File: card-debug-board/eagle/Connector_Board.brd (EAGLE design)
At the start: 62 x 34 mm, 39 parts, among them J1 ORESAT-DEBUG-CONNECTOR-CARD, J3 USB_A_SMT_FEMALE, Q1 MOSFET-PCH-SOT23-6, SW1 B3F-1000, U1 FT230XS-R

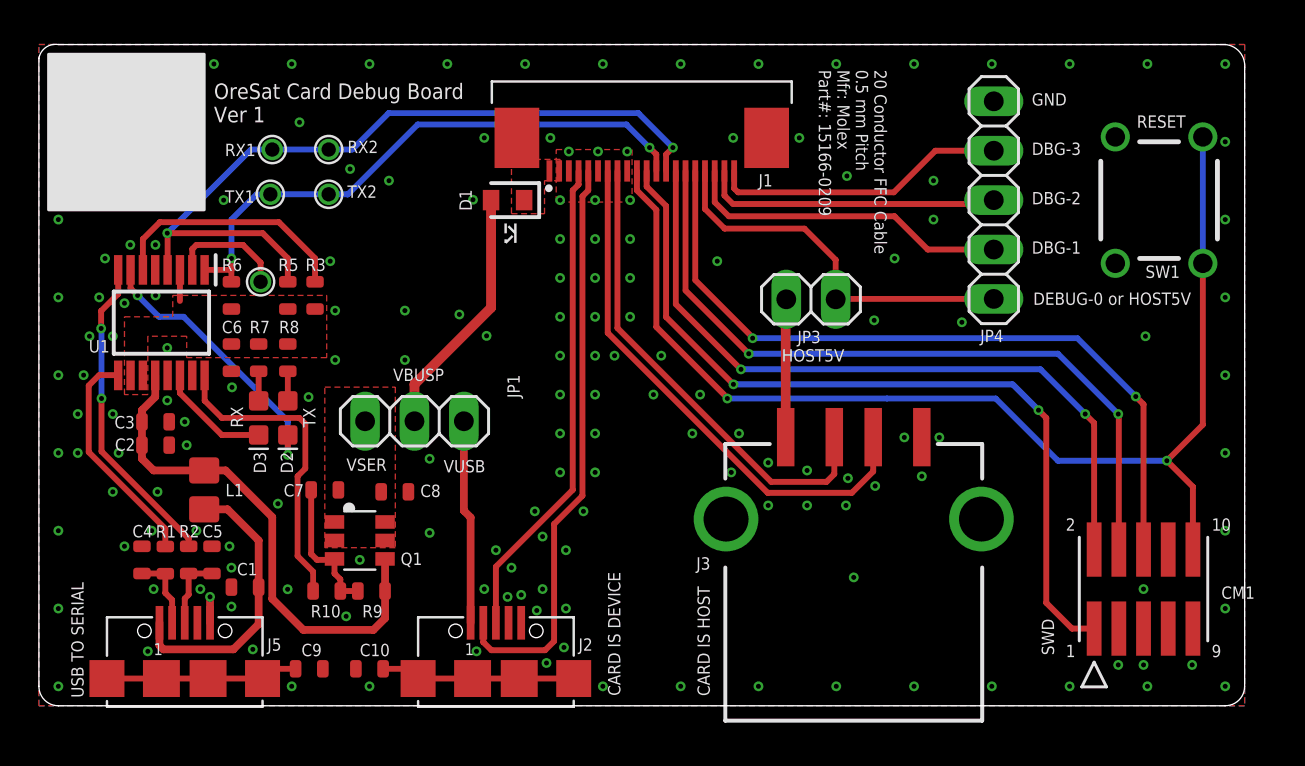
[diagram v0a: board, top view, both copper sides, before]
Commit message: Re-Done with mirrored edge connector
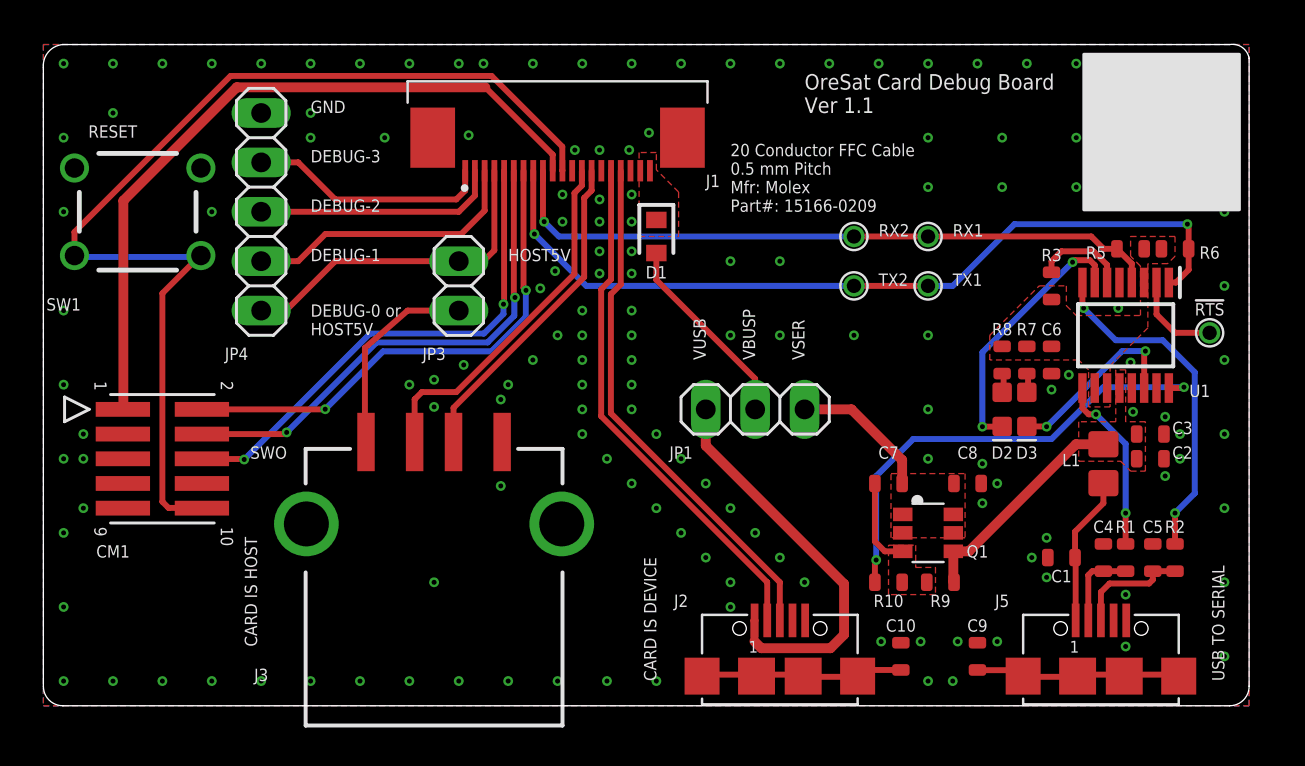
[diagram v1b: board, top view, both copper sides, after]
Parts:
- J1: value ORESAT-DEBUG-CONNECTOR-CARD -> ORESAT-DEBUG-CONNECTOR-MIRRORED-CARD; device oresat-edge_connector:TE_2-1734592-0 -> oresat-debug-connector:TE_2-1734592-0
- moved SW1 52.5 mm to (5.08, 25.4), turned to 0 degrees
- moved C2 51.2 mm to (57.1, 12.7)
- moved C3 51.2 mm to (57.1, 14.0)
- moved CM1 50.9 mm to (6.35, 12.7), turned to 270 degrees
- moved R2 50.7 mm to (58.4, 7.62)
- moved U1 49.6 mm to (55.9, 19.1)
- moved C4 49.4 mm to (54.7, 7.62)
- moved R1 49.4 mm to (55.9, 7.62)
- moved !RTS 48.9 mm to (60.2, 19.2)
- moved R6 48.6 mm to (58.4, 23.5), turned to 180 degrees
- moved C5 48.4 mm to (57.3, 7.62)
- moved J5 47.1 mm to (54.6, 1.52)
- moved L1 46.3 mm to (54.7, 12.4)
- moved R5 43.4 mm to (56.1, 23.5), turned to 0 degrees
- moved C6 42.2 mm to (52.1, 17.8)
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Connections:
- net DEBUG-0/HOST5V: now also J1.4; no longer J1.17
- net DEBUG-1: now also J1.3; no longer J1.18
- net DEBUG-2: now also J1.2; no longer J1.19
- net DEBUG-3: now also J1.1; no longer J1.20
- net GND: now also J1.12, J1.15, J1.18; no longer J1.3, J1.6, J1.9
- net HOSTD_N: now also J1.13; no longer J1.8
- net HOSTD_P: now also J1.14; no longer J1.7
- net NRST: now also J1.11; no longer J1.10
- net RXD: now also J1.9; no longer J1.13
- net SWCLK: now also J1.6; no longer J1.15
- net SWDIO: now also J1.7; no longer J1.14
- net SWO: now also J1.5; no longer J1.16
- net TXD: now also J1.8; no longer J1.12
- net USB-DEVICE_D_N: now also J1.16; no longer J1.5
- net USB-DEVICE_D_P: now also J1.17; no longer J1.4
- net VBUSP: now also J1.19, J1.20; no longer J1.1, J1.2
- net VTARGET: now also J1.10; no longer J1.11
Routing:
- net VCC: track 26.5 -> 11.6 mm
- net TXD: track 30.0 -> 42.9 mm
- net SWO: track 38.8 -> 26.0 mm
- net SWCLK: track 38.0 -> 26.1 mm
- net SWDIO: track 37.4 -> 26.2 mm
- net HOSTD_P: track 27.6 -> 16.9 mm
- net VUSB: track 10.5 -> 20.7 mm
- net CTS#: track 12.8 -> 4.83 mm
- net PWREN#: track 16.1 -> 24.0 mm, vias 0 -> 2
- net VSER: track 0.00 -> 7.30 mm
- net VBUS_UART: track 14.6 -> 7.67 mm
- net HOSTD_N: track 24.6 -> 18.5 mm
- net RXD: track 40.5 -> 34.7 mm, vias 2 -> 1
- net NRST: track 60.1 -> 54.6 mm, vias 2 -> 0
- net VTARGET: track 42.1 -> 37.5 mm, vias 2 -> 0
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- added copper zone on layer 1, net N$3
- added copper zone on layer 1, net VCC
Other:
- outline, holes or cut-outs redrawn
- board text added: "DEBUG-1"
- board text added: "DEBUG-2"
- board text added: "DEBUG-3"
- board text added: "OreSat Card Debug Board Ver 1.1"
- board text added: "SWO"
- board text removed: "DBG-1"
- board text removed: "DBG-2"
- board text removed: "DBG-3"
- board text removed: "OreSat Card Debug Board Ver 1"
- board text removed: "SWD"

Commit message: Clean up text , added gnd via's
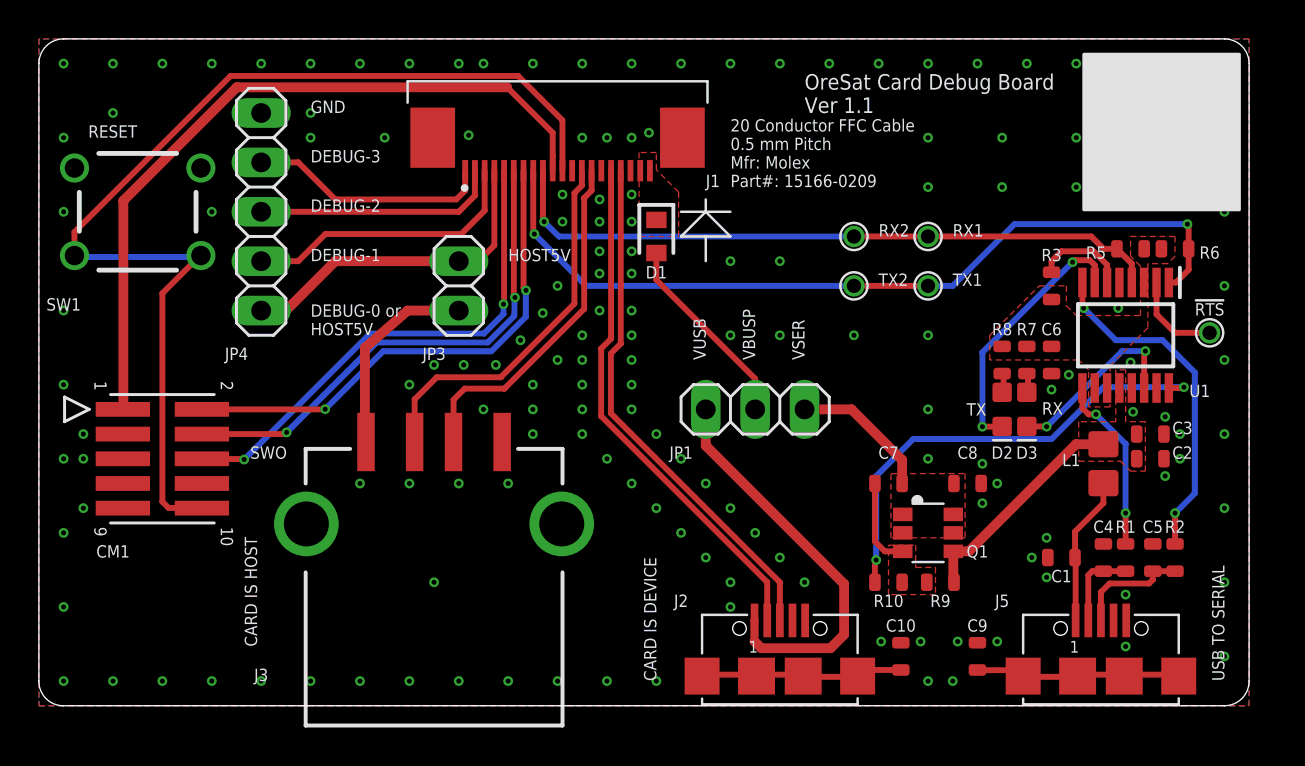
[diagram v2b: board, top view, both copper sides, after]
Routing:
- net HOSTD_P: track 16.9 -> 18.1 mm
- net HOSTD_N: track 18.5 -> 19.4 mm
- net NRST: track 54.6 -> 55.4 mm
- net VTARGET: track 37.5 -> 38.1 mm
- net GND: vias 150 -> 155
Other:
- board size 62 x 34 mm -> 62.2 x 34.3 mm
- board text removed: "Connector Clearance"

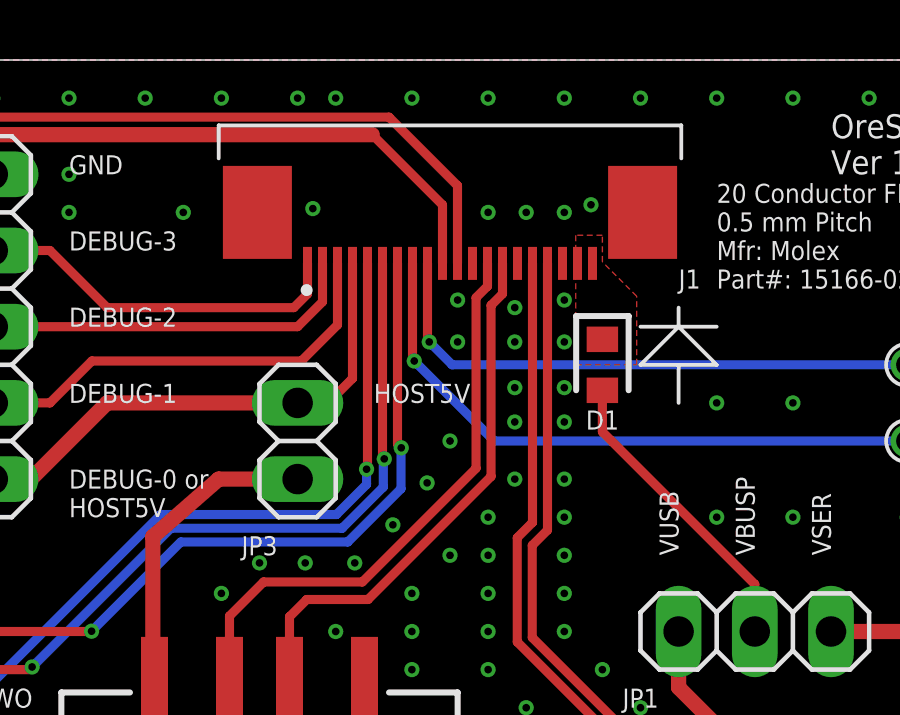
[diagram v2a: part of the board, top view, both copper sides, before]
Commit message: Switched to thin mirrored edge connector
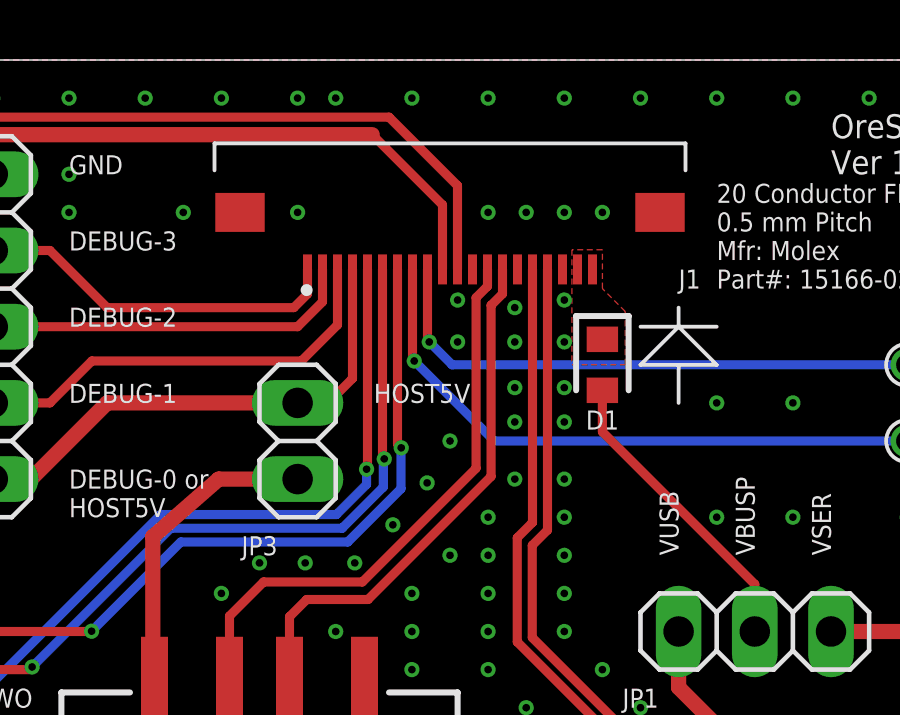
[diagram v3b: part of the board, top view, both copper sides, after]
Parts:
- J1: value ORESAT-DEBUG-CONNECTOR-MIRRORED-CARD -> ORESAT-DEBUG-CONNECTOR-MIRRORED-SOLAR; device oresat-debug-connector:TE_2-1734592-0 -> oresat-debug-connector:WURTH_687120183622
